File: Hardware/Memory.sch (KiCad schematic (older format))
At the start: 4 parts, among them U2 AS7C34098A, X3 SDBMF

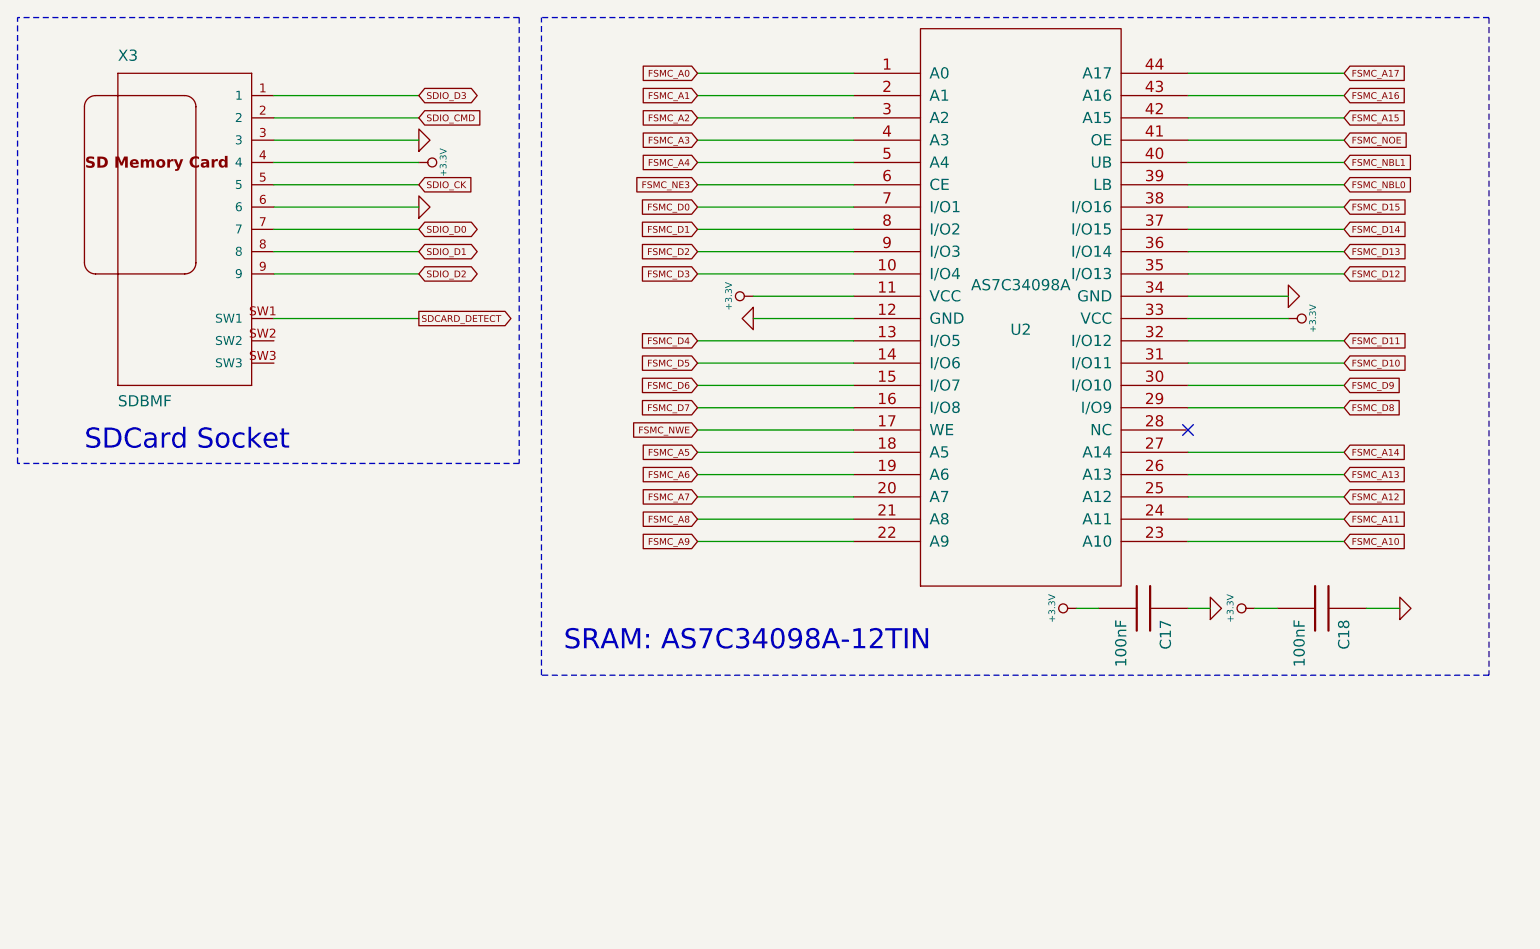
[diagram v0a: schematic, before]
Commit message: Created PCB for new version with parallel display & sram
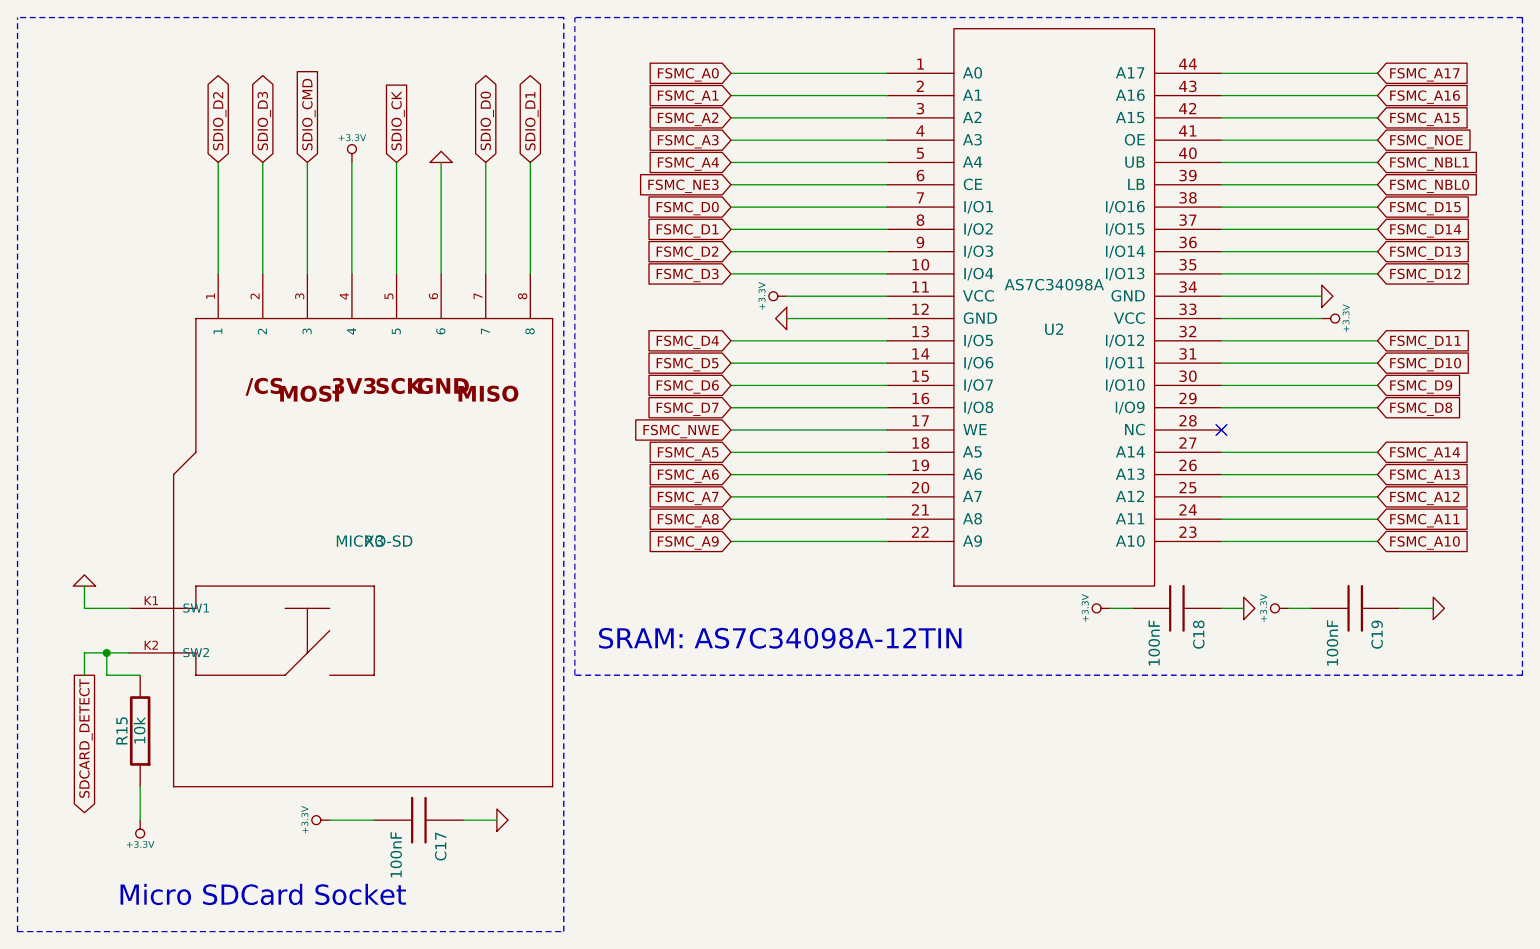
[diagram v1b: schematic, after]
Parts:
- removed X3: SDBMF, farnell-SDBMF-009XXBXX2, symbol SDBMF
- added C17: 100nF, symbol C
- added R15: 10k, symbol R
- added X3: MICRO-SD, welectronic-MICRO-SD, symbol MICRO-SD
- renumbered C17 to C18, C18 to C19
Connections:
- net +3.3V: now also C17.2, R15.1, X3.4
- net GND: now also C17.1, X3.6, X3.K1 (SW1)
- net SDCARD_DETECT: now also R15.2, X3.K2 (SW2)
- net SDIO_CK: now also X3.5
- net SDIO_CMD: now also X3.3
- net SDIO_D0: now also X3.7
- net SDIO_D1: now also X3.8
- net SDIO_D2: now also X3.1
- net SDIO_D3: now also X3.2
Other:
- note added: "Micro SDCard Socket"
- note removed: "SDCard Socket"
- moved on the sheet: C18, C19, U2
